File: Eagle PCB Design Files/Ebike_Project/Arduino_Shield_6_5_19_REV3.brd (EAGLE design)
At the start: 160 x 100 mm, 8 parts

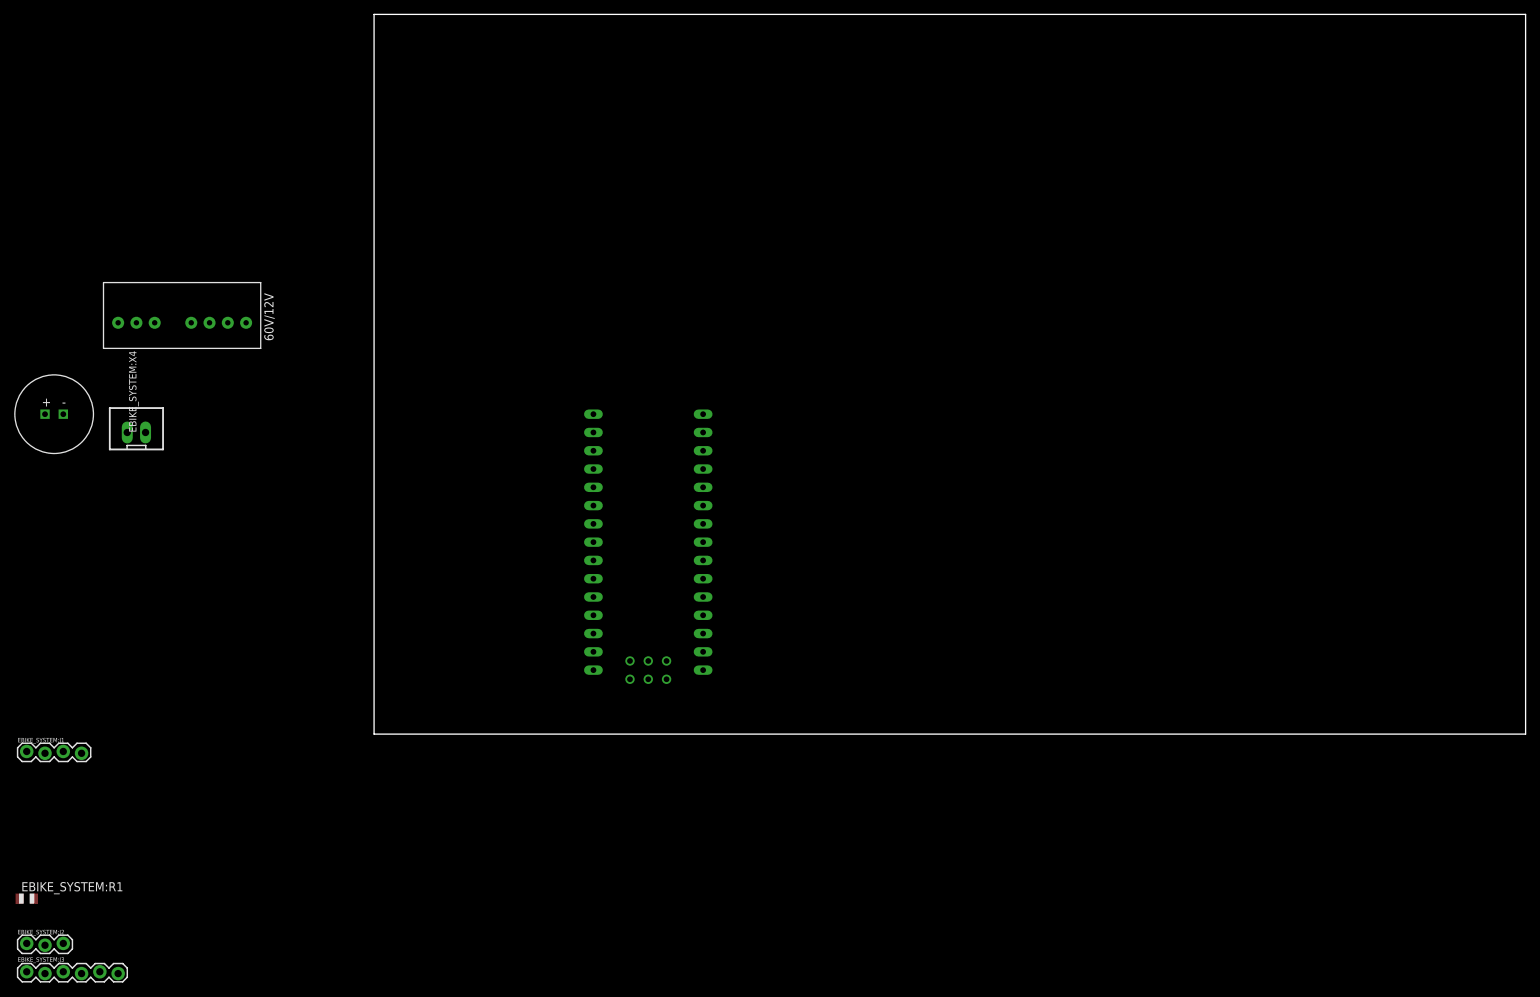
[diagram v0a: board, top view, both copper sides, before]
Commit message: Completed REV3 of board
REV adds a larger DC/DC converter and connector for a 12V headlight
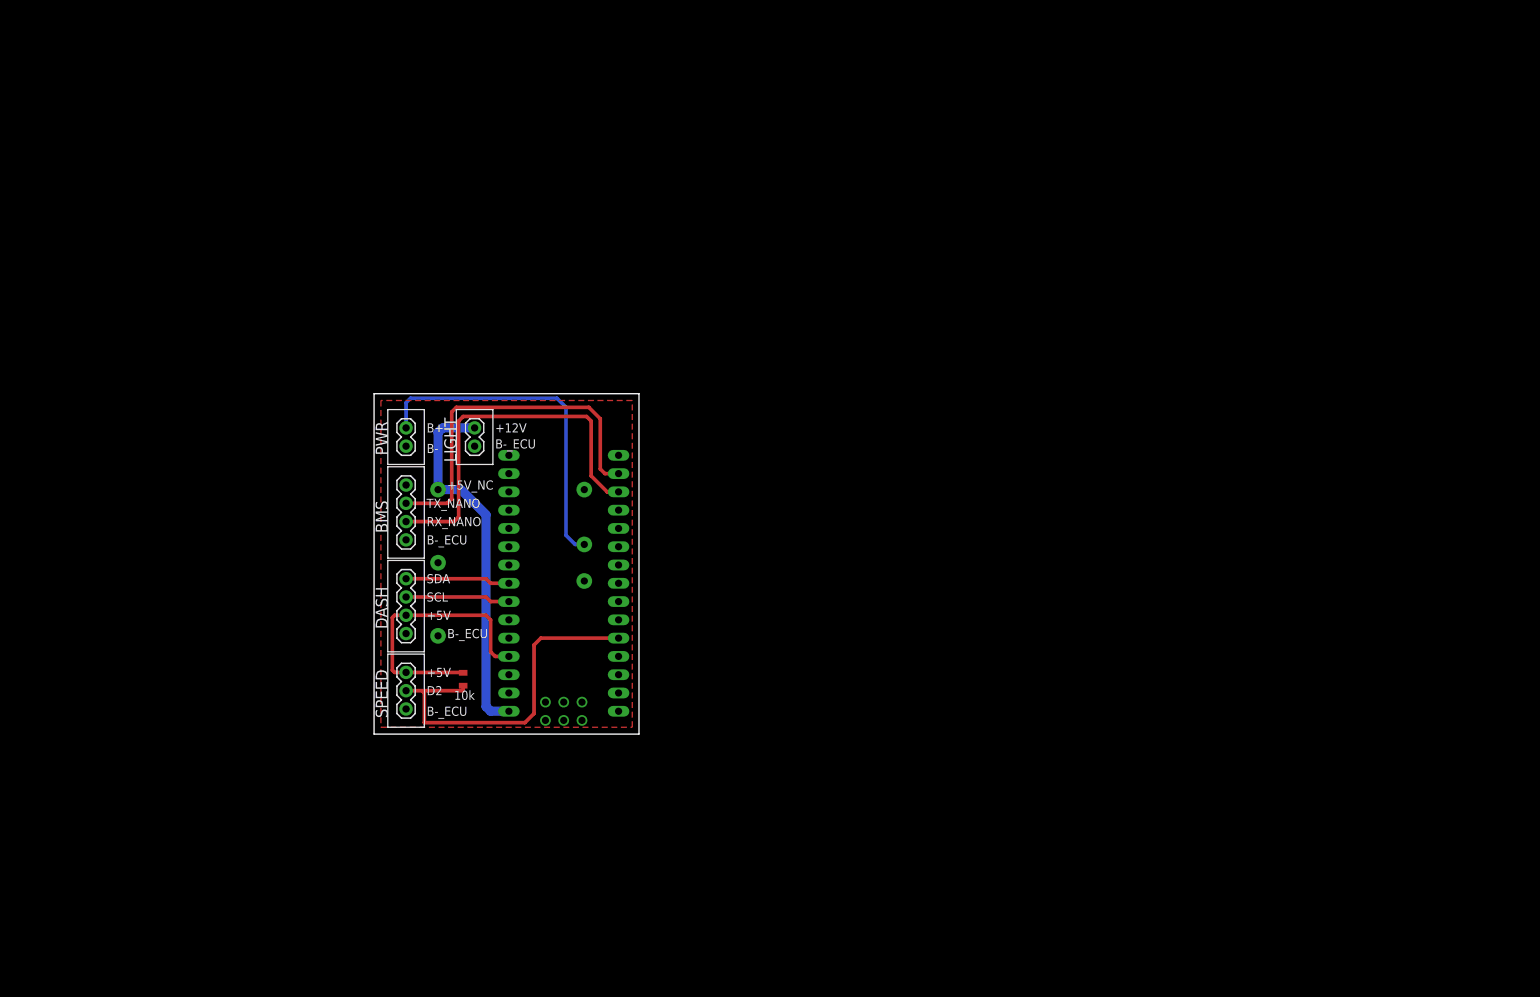
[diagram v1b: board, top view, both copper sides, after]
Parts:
- removed EBIKE_SYSTEM:J1: (no value), SparkFun-Connectors:1X04_LOCK
- removed EBIKE_SYSTEM:J2: (no value), SparkFun-Connectors:1X03_LOCK
- removed EBIKE_SYSTEM:J3: (no value), SparkFun-Connectors:1X06_LOCK
- removed EBIKE_SYSTEM:R1: 10k, adafruit:R0805
- removed EBIKE_SYSTEM:U$1: NANO, Arduino-clone:NANO
- removed EBIKE_SYSTEM:U$2: SPBW06G-12, Bryan's_Library:SPBW06G-12
- removed EBIKE_SYSTEM:U$3: THROUGHHOLE_CAP, Bryan's_Library:THROUGHHOLE_CAP
- removed EBIKE_SYSTEM:X4: JST_XH_02, Rembrandt Electronics - JST XH Connectors v1-0:JST-XH-02-PACKAGE-LONG-PAD
- added ECU:BMS, ECU:DASH: 4PIN_CONN, EBike_Project_Library:1X04
- added ECU:HALL-SENSOR: 3PIN_CONN, EBike_Project_Library:1X03
- added ECU:HEADLIGHT, ECU:POWER: 2PIN_CONN, EBike_Project_Library:1X02
- added ECU:R1: 10k, EBike_Project_Library:0805
- added ECU:U$1: NANO, EBike_Project_Library:NANO
- added ECU:U$2: SKM15C-12_DCDC, EBike_Project_Library:SKM15C-12_DCDC
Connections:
- removed net EBIKE_SYSTEM:+12V_IN: EBIKE_SYSTEM:U$1.RAW, EBIKE_SYSTEM:U$3.+
- removed net EBIKE_SYSTEM:+12V_OUT: EBIKE_SYSTEM:U$2.+V_OUT
- removed net EBIKE_SYSTEM:12V_IN: EBIKE_SYSTEM:J3.1
- removed net EBIKE_SYSTEM:12V_OUT: EBIKE_SYSTEM:J3.2
- removed net EBIKE_SYSTEM:5V_VCC_RED: EBIKE_SYSTEM:J3.4, EBIKE_SYSTEM:U$1.5V
- removed net EBIKE_SYSTEM:B+: EBIKE_SYSTEM:U$2.+V_IN, EBIKE_SYSTEM:X4.1
- removed net EBIKE_SYSTEM:GND_BLACK: EBIKE_SYSTEM:J3.3
- removed net EBIKE_SYSTEM:LCD_SCL_BLUE: EBIKE_SYSTEM:J3.5, EBIKE_SYSTEM:U$1.A5
- removed net EBIKE_SYSTEM:LCD_SDA_GREEN: EBIKE_SYSTEM:J3.6, EBIKE_SYSTEM:U$1.A4
- removed net EBIKE_SYSTEM:N$1: EBIKE_SYSTEM:J1.1
- removed net N$4: EBIKE_SYSTEM:J2.2, EBIKE_SYSTEM:R1.1, EBIKE_SYSTEM:U$1.D2
- removed net N$7: EBIKE_SYSTEM:J1.3, EBIKE_SYSTEM:U$1.D10
- removed net N$8: EBIKE_SYSTEM:J1.2, EBIKE_SYSTEM:U$1.D11
- removed net N$9: EBIKE_SYSTEM:J1.4, EBIKE_SYSTEM:J2.3, EBIKE_SYSTEM:U$1.GND, EBIKE_SYSTEM:U$2.-V_IN, EBIKE_SYSTEM:U$2.-V_OUT, EBIKE_SYSTEM:U$3.-, EBIKE_SYSTEM:X4.2
- new net +12V: ECU:HEADLIGHT.2, ECU:U$1.RAW, ECU:U$2.+VOUT
- new net +5V: ECU:DASH.2, ECU:HALL-SENSOR.1, ECU:R1.2, ECU:U$1.5V
- new net B+: ECU:POWER.2, ECU:U$2.+VIN
- new net B-_ECU: ECU:BMS.4, ECU:DASH.1, ECU:HALL-SENSOR.3, ECU:HEADLIGHT.1, ECU:POWER.1, ECU:U$1.GND, ECU:U$2.-VIN, ECU:U$2.-VOUT
- new net LCD_SCL: ECU:DASH.3, ECU:U$1.A5
- new net LCD_SDA: ECU:DASH.4, ECU:U$1.A4
- new net RX_NANO: ECU:BMS.3, ECU:U$1.D10
- new net TX_NANO: ECU:BMS.2, ECU:U$1.D11
- net N$3: now also ECU:HALL-SENSOR.2, ECU:R1.1, ECU:U$1.D2; no longer EBIKE_SYSTEM:J2.1, EBIKE_SYSTEM:R1.2
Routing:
- net RX_NANO: track 0.00 -> 52.2 mm
- net +12V: track 0.00 -> 51.5 mm
- net N$3: track 0.00 -> 50.6 mm
- net TX_NANO: track 0.00 -> 50.0 mm
- net B+: track 0.00 -> 47.3 mm
- net +5V: track 0.00 -> 38.6 mm
- net LCD_SDA: track 0.00 -> 14.6 mm
- net LCD_SCL: track 0.00 -> 14.6 mm
- added copper zone on layer 1, net B-_ECU
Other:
- board size 160 x 100 mm -> 36.8 x 47.3 mm
- board text added: "+12V"
- board text added: "+5V"
- board text added: "+5V_NC"
- board text added: "10k"
- board text added: "36-72V/12V"
- board text added: "B+"
- board text added: "B-"
- board text added: "B-_ECU"
- board text added: "BMS"
- board text added: "Bryan Ford"
- board text added: "D2"
- board text added: "DASH"
- board text added: "EBIKE SPEEDOMETER/BMS INTERFACE"
- board text added: "LIGHT"
- board text added: "PWR"
- board text added: "REV3 6_21_19"
- board text added: "RX_NANO"
- board text added: "SCL"
- board text added: "SDA"
- board text added: "SKM15C-12"
- board text added: "SPEED"
- board text added: "TX_NANO"

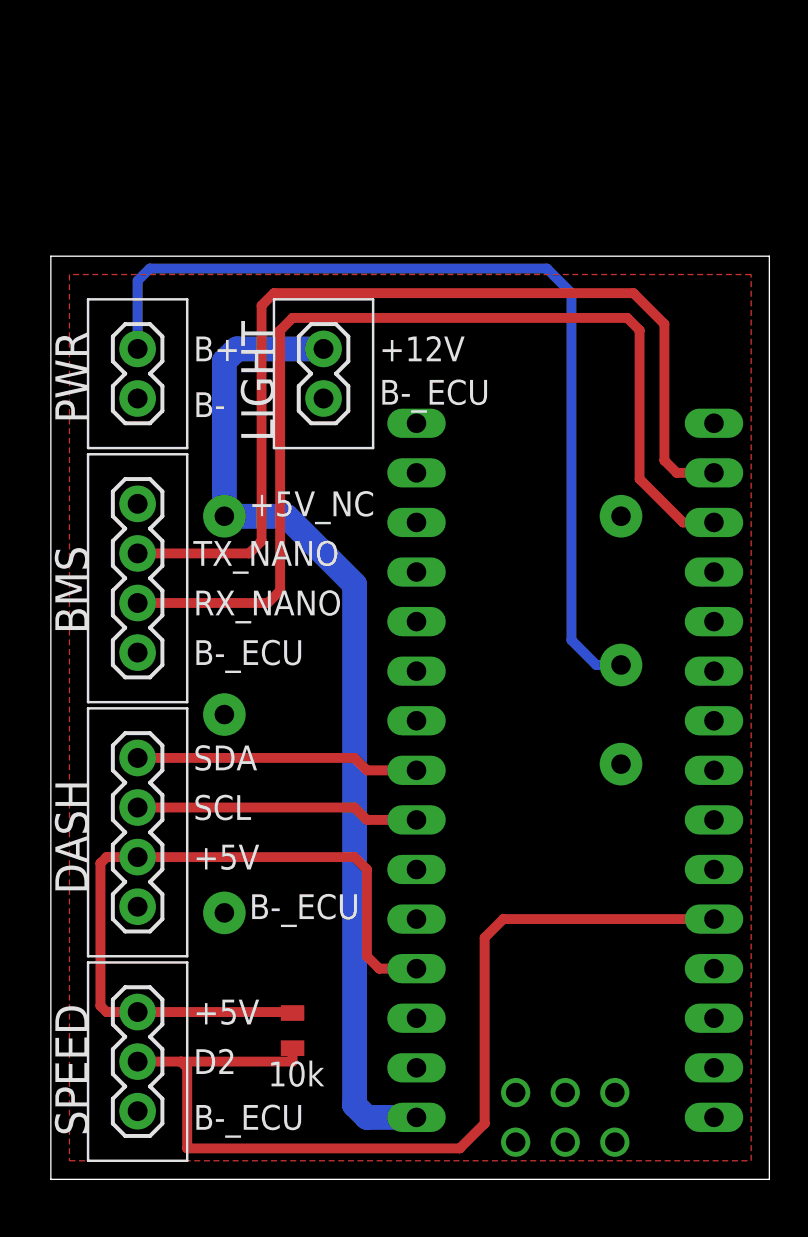
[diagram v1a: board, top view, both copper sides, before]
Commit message: Completed REV3
REV3 is identical to REV4 but uses an off the shelf arduino nano.
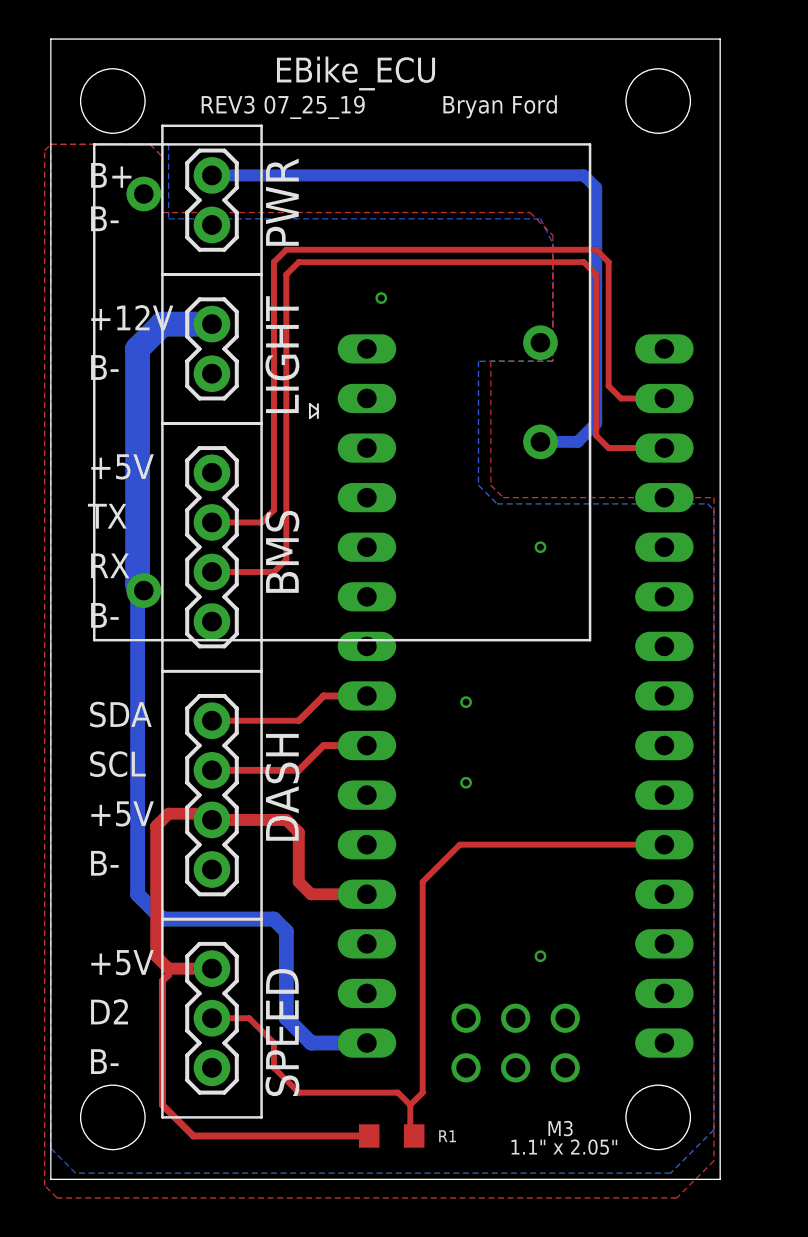
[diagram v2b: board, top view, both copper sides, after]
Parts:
- removed ECU:BMS, ECU:DASH: 4PIN_CONN, EBike_Project_Library:1X04
- removed ECU:HALL-SENSOR: 3PIN_CONN, EBike_Project_Library:1X03
- removed ECU:HEADLIGHT, ECU:POWER: 2PIN_CONN, EBike_Project_Library:1X02
- removed ECU:R1: 10k, EBike_Project_Library:0805
- removed ECU:U$1: NANO, EBike_Project_Library:NANO
- removed ECU:U$2: SKM15C-12_DCDC, EBike_Project_Library:SKM15C-12_DCDC
- added CXTR_BMS, CXTR_DASH: 4PIN_.1"_CONNECTOR, EBike_Project_Library:1X04
- added CXTR_HALL_SENSOR: 3PIN_.1"_CONNECTOR, EBike_Project_Library:1X03
- added CXTR_HEADLIGHT, CXTR_POWER: 2PIN_.1"_CONNECTOR, EBike_Project_Library:1X02
- added R1: 4.99, EBike_Project_Library:0805
- added U$2: SKM15C-12_DCDC, EBike_Project_Library:SKM15C-12_DCDC
- added U$3: ARDUINO_NANO, EBike_Project_Library:NANO
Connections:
- removed net LCD_SCL: ECU:DASH.3, ECU:U$1.A5
- removed net LCD_SDA: ECU:DASH.4, ECU:U$1.A4
- removed net N$3: ECU:HALL-SENSOR.2, ECU:R1.1, ECU:U$1.D2
- removed net RX_NANO: ECU:BMS.3, ECU:U$1.D10
- removed net TX_NANO: ECU:BMS.2, ECU:U$1.D11
- new net D2_HALL: CXTR_HALL_SENSOR.2, R1.1, U$3.D2
- new net LCD_SCL_A5: CXTR_DASH.3, U$3.A5
- new net LCD_SDA_A4: CXTR_DASH.4, U$3.A4
- new net RX_NANO_D10: CXTR_BMS.3, U$3.D10
- new net TX_NANO_D11: CXTR_BMS.2, U$3.D11
- net +12V: now also CXTR_HEADLIGHT.2, U$2.+VOUT, U$3.RAW; no longer ECU:HEADLIGHT.2, ECU:U$1.RAW, ECU:U$2.+VOUT
- net +5V: now also CXTR_DASH.2, CXTR_HALL_SENSOR.1, R1.2, U$3.5V; no longer ECU:DASH.2, ECU:HALL-SENSOR.1, ECU:R1.2, ECU:U$1.5V
- net B+: now also CXTR_POWER.2, U$2.+VIN; no longer ECU:POWER.2, ECU:U$2.+VIN
- net B-_ECU: now also CXTR_BMS.4, CXTR_DASH.1, CXTR_HALL_SENSOR.3, CXTR_HEADLIGHT.1, CXTR_POWER.1, U$2.-VIN, U$2.-VOUT, U$3.GND; no longer ECU:BMS.4, ECU:DASH.1, ECU:HALL-SENSOR.3, ECU:HEADLIGHT.1, ECU:POWER.1, ECU:U$1.GND, ECU:U$2.-VIN, ECU:U$2.-VOUT
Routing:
- net RX_NANO: track 52.2 -> 0.00 mm
- net N$3: track 50.6 -> 0.00 mm
- net TX_NANO: track 50.0 -> 0.00 mm
- net RX_NANO_D10: track 0.00 -> 47.1 mm
- net TX_NANO_D11: track 0.00 -> 43.3 mm
- net D2_HALL: track 0.00 -> 39.3 mm
- net LCD_SDA: track 14.6 -> 0.00 mm
- net LCD_SCL: track 14.6 -> 0.00 mm
- net B+: track 47.3 -> 35.3 mm
- net LCD_SCL_A5: track 0.00 -> 8.46 mm
- net LCD_SDA_A4: track 0.00 -> 8.46 mm
- net +5V: track 38.6 -> 42.4 mm
- net +12V: track 51.5 -> 50.2 mm
- added copper zone on layer 16, net B-_ECU
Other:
- board size 36.8 x 47.3 mm -> 34.3 x 58.4 mm
- board text added: "0"
- board text added: "1"
- board text added: "1.1" x 2.05""
- board text added: "10"
- board text added: "2"
- board text added: "3"
- board text added: "3V3"
- board text added: "4"
- board text added: "5"
- board text added: "5V_REF"
- board text added: "6"
- board text added: "7"
- board text added: "8"
- board text added: "9"
- board text added: "A0"
- board text added: "A1"
- board text added: "A2"
- board text added: "A3"
- board text added: "A4"
- board text added: "A5"
- board text added: "A6"
- board text added: "A7"
- board text added: "AREF"
- board text added: "DC_VIN+"
- board text added: "DC_VIN-"
- board text added: "EBike_ECU"
- board text added: "GND1"
- board text added: "ISP1_1"
- board text added: "ISP1_3"
- board text added: "ISP1_4"
- board text added: "ISP1_5"
- board text added: "M3"
- board text added: "NANO TEST POINTS"
- board text added: "RESET"
- board text added: "REV3 07_25_19"
- board text added: "RX"
- board text added: "TX"
- board text added: "USB_5V"
- board text added: "USB_D+"
- board text added: "USB_D-"
- board text added: "USB_GND"
- board text removed: "+5V_NC"
- board text removed: "10k"
- board text removed: "B-_ECU"
- board text removed: "EBIKE SPEEDOMETER/BMS INTERFACE"
- board text removed: "REV3 6_21_19"
- board text removed: "RX_NANO"
- board text removed: "TX_NANO"
